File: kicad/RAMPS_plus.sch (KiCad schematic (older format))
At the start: 7 parts

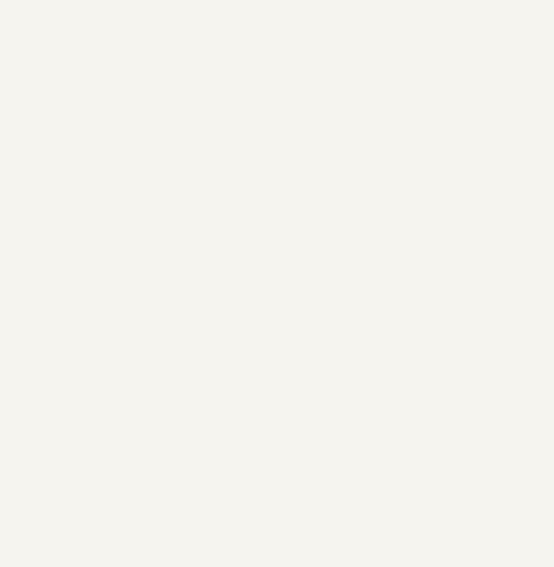
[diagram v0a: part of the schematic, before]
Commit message: Draw schematic
Added 40109 translators to drive MOSFET's.

References: #1 #5 #13 #9
Close #6
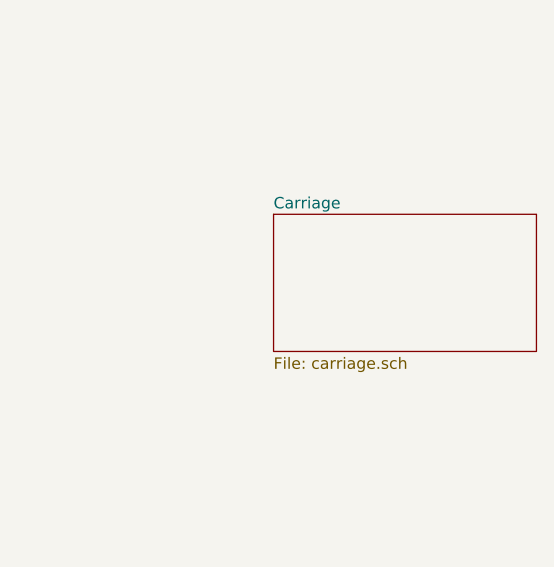
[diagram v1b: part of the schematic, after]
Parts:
- gave numbers to parts that had none: 7
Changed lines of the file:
@@
 EESchema Schematic File Version 2
 LIBS:CircuitHub
+LIBS:power
+LIBS:transistors
+LIBS:regul
+LIBS:device
 LIBS:RAMPS_plus-cache
 EELAYER 27 0
@@
 $Descr A4 11693 8268
 encoding utf-8
-Sheet 1 1
+Sheet 1 2
 Title "Ramps plus"
-Date "8 apr 2014"
+Date "15 apr 2014"
 Rev "1.0"
 Comp "peter@7408hacks.com"
@@
 $EndDescr
 $Comp
-L "1788-61300811121" P?
+L "1788-61300811121" P2
 U 1 1 53430C34
 P 2400 1600
-F 0 "P?" H 2400 1630 60  0000 L CNN
+F 0 "P2" H 2400 1630 60  0000 L CNN
 F 1 "\"1788-61300811121\"" H 2400 670 60  0000 L CNN
 F 2 "7408hacks/dibfv" H 2400 1900 60  0001 L CNN
@@
 $EndComp
 $Comp
-L "1788-61300811121" P?
+L "1788-61300811121" P3
 U 1 1 53430C53
 P 2400 2700
-F 0 "P?" H 2400 2730 60  0000 L CNN
+F 0 "P3" H 2400 2730 60  0000 L CNN
 F 1 "\"1788-61300811121\"" H 2400 1770 60  0000 L CNN
 F 2 "7408hacks/dibfv" H 2400 3000 60  0001 L CNN
@@
 $EndComp
 $Comp
-L "1788-61300811121" P?
+L "1788-61300811121" P4
 U 1 1 53430C72
 P 2400 3800
-F 0 "P?" H 2400 3830 60  0000 L CNN
+F 0 "P4" H 2400 3830 60  0000 L CNN
 F 1 "\"1788-61300811121\"" H 2400 2870 60  0000 L CNN
 F 2 "7408hacks/dibfv" H 2400 4100 60  0001 L CNN
@@
 $EndComp
 $Comp
-L "1788-61300811121" P?
+L "1788-61300811121" P6
 U 1 1 53430C91
 P 2700 2700
-F 0 "P?" H 2700 2730 60  0000 L CNN
+F 0 "P6" H 2700 2730 60  0000 L CNN
 F 1 "\"1788-61300811121\"" H 2700 1770 60  0000 L CNN
 F 2 "7408hacks/dibfv" H 2700 3000 60  0001 L CNN
@@
 $EndComp
 $Comp
-L "1788-61300811121" P?
+L "1788-61300811121" P7
 U 1 1 53430CB0
 P 2700 3800
-F 0 "P?" H 2700 3830 60  0000 L CNN
+F 0 "P7" H 2700 3830 60  0000 L CNN
 F 1 "\"1788-61300811121\"" H 2700 2870 60  0000 L CNN
 F 2 "7408hacks/dibfv" H 2700 4100 60  0001 L CNN
@@
 $EndComp
 $Comp
-L "1789-61301011121" P?
+L "1789-61301011121" P5
 U 1 1 53430CCF
 P 2700 1400
-F 0 "P?" H 2700 1430 60  0000 L CNN
+F 0 "P5" H 2700 1430 60  0000 L CNN
 F 1 "\"1789-61301011121\"" H 2700 270 60  0000 L CNN
 F 2 "7408hacks/dio2r" H 2700 1700 60  0001 L CNN
@@
 $EndComp
 $Comp
-L "1790-61303621121" P?
+L "1790-61303621121" P1
 U 1 1 534310C0
 P 2200 4900
-F 0 "P?" H 2200 4930 60  0000 L CNN
+F 0 "P1" H 2200 4930 60  0000 L CNN
 F 1 "\"1790-61303621121\"" H 2200 2970 60  0000 L CNN
 F 2 "7408hacks/dio2z" H 2200 5200 60  0001 L CNN
@@
 Wire Notes Line
 	3850 1050 1200 1050
+$Sheet
+S 5200 2000 1150 600
+U 534454B0
+F0 "Carriage" 50
+F1 "carriage.sch" 50
+$EndSheet
 $EndSCHEMATC

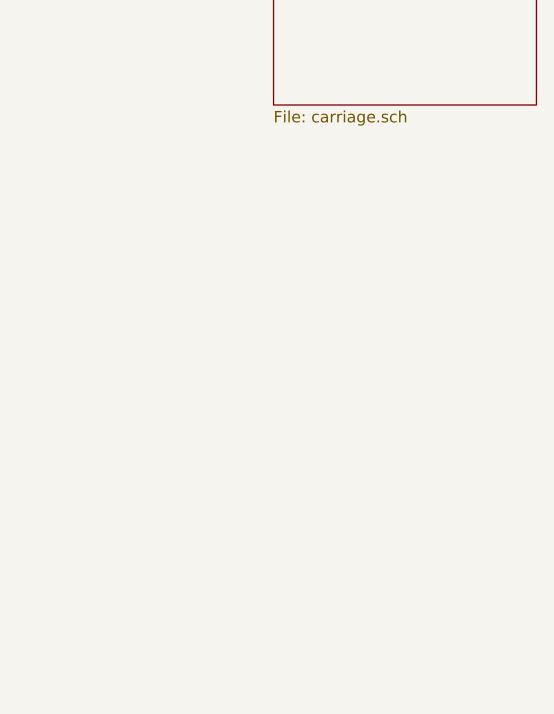
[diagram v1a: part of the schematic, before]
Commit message: Draw schematic
Added sheet for panel connector and sheet for Y axis circuits.
Added ULN2803

References: #1 #11 #7 #5
Close #13
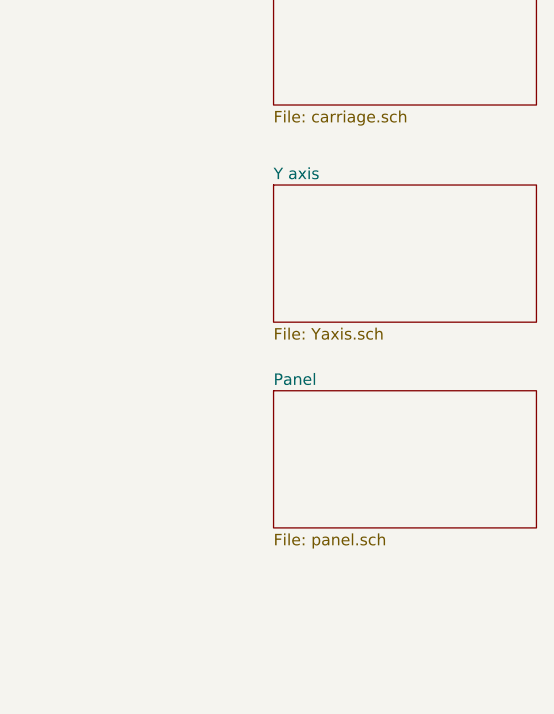
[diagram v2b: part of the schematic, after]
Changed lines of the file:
@@
 LIBS:CircuitHub
 LIBS:power
-LIBS:transistors
 LIBS:regul
 LIBS:device
+LIBS:opto
+LIBS:transistor
 LIBS:RAMPS_plus-cache
 EELAYER 27 0
@@
 $Descr A4 11693 8268
 encoding utf-8
-Sheet 1 2
+Sheet 1 4
 Title "Ramps plus"
-Date "15 apr 2014"
+Date "16 apr 2014"
 Rev "1.0"
 Comp "peter@7408hacks.com"
@@
 F1 "carriage.sch" 50
 $EndSheet
+$Sheet
+S 5200 2950 1150 600
+U 534EC4C7
+F0 "Y axis" 50
+F1 "Yaxis.sch" 50
+$EndSheet
+$Sheet
+S 5200 3850 1150 600
+U 534EE32B
+F0 "Panel" 50
+F1 "panel.sch" 50
+$EndSheet
 $EndSCHEMATC

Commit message: Draw schematic
Finished redrawing basic RAMPS schematic

References: #1 #4 #7 #15
Close #5 #17 #18
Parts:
- added C11, C12, C13: 100n/50V, 0603, symbol C
- added D5: N.C., 7408hacks/dibfu, symbol "1851-SS54"
- added D6, D7, D8, D9: \"1851-SS54\", 7408hacks/dibfu, symbol "1851-SS54"
- added F1, F2, F3, F4: FUSE, symbol FUSE
- added P18: CONN_6, symbol CONN_6
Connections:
- net labels added: +12V, Vbed, Vheat, Vmot
- wire segments 77 -> 117
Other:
- note added: "Littelfuse MINI Blade Fuse\nmodel 0297015 (15A)\n% of rating | opening time max\n135% | 600s\n200% | 5 s \n350% | 0.25 s \n600% | 0.1 s"

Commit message: Change components to my own
References: #1 #19
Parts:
- removed D5: N.C., 7408hacks/dibfu, symbol "1851-SS54"
- removed D6, D7, D8, D9: \"1851-SS54\", 7408hacks/dibfu, symbol "1851-SS54"
- removed F1, F2, F3, F4: FUSE, symbol FUSE
- removed P1: \"1790-61303621121\", 7408hacks/dio2z, symbol "1790-61303621121"
- removed P18: CONN_6, symbol CONN_6
- removed P2, P3, P4, P6, P7: \"1788-61300811121\", 7408hacks/dibfv, symbol "1788-61300811121"
- removed P5: \"1789-61301011121\", 7408hacks/dio2r, symbol "1789-61301011121"
- added CON1: CON10, symbol CON10
- added CON2, CON3, CON4, CON5, CON6: CON8, symbol CON8
- added CON7: CON18x2, symbol CON18x2
- added CON?: CON6, symbol CON6
- added D1, D2, D3, D4, D5: SS54, SMC, symbol SS54
- added F1, F2, F3, F4: MINI_Blade_Fuse_Holder, Littlefuse_01530008, symbol MINI_Blade_Fuse_Holder
- renumbered C11 to C1, C12 to C2, C13 to C3
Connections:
- wire segments 117 -> 130
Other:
- note added: "Littelfuse MINI Blade Fuse\nmodel 0297015 (15A)\n% of rating | opening time max\n135% | 600s\n200% | 5 s \n350% | 0.25 s \n600% | 0.1 s\nReverse protection diode should \nwithstand at least 50A for 0.3s."
- note removed: "Littelfuse MINI Blade Fuse\nmodel 0297015 (15A)\n% of rating | opening time max\n135% | 600s\n200% | 5 s \n350% | 0.25 s \n600% | 0.1 s"

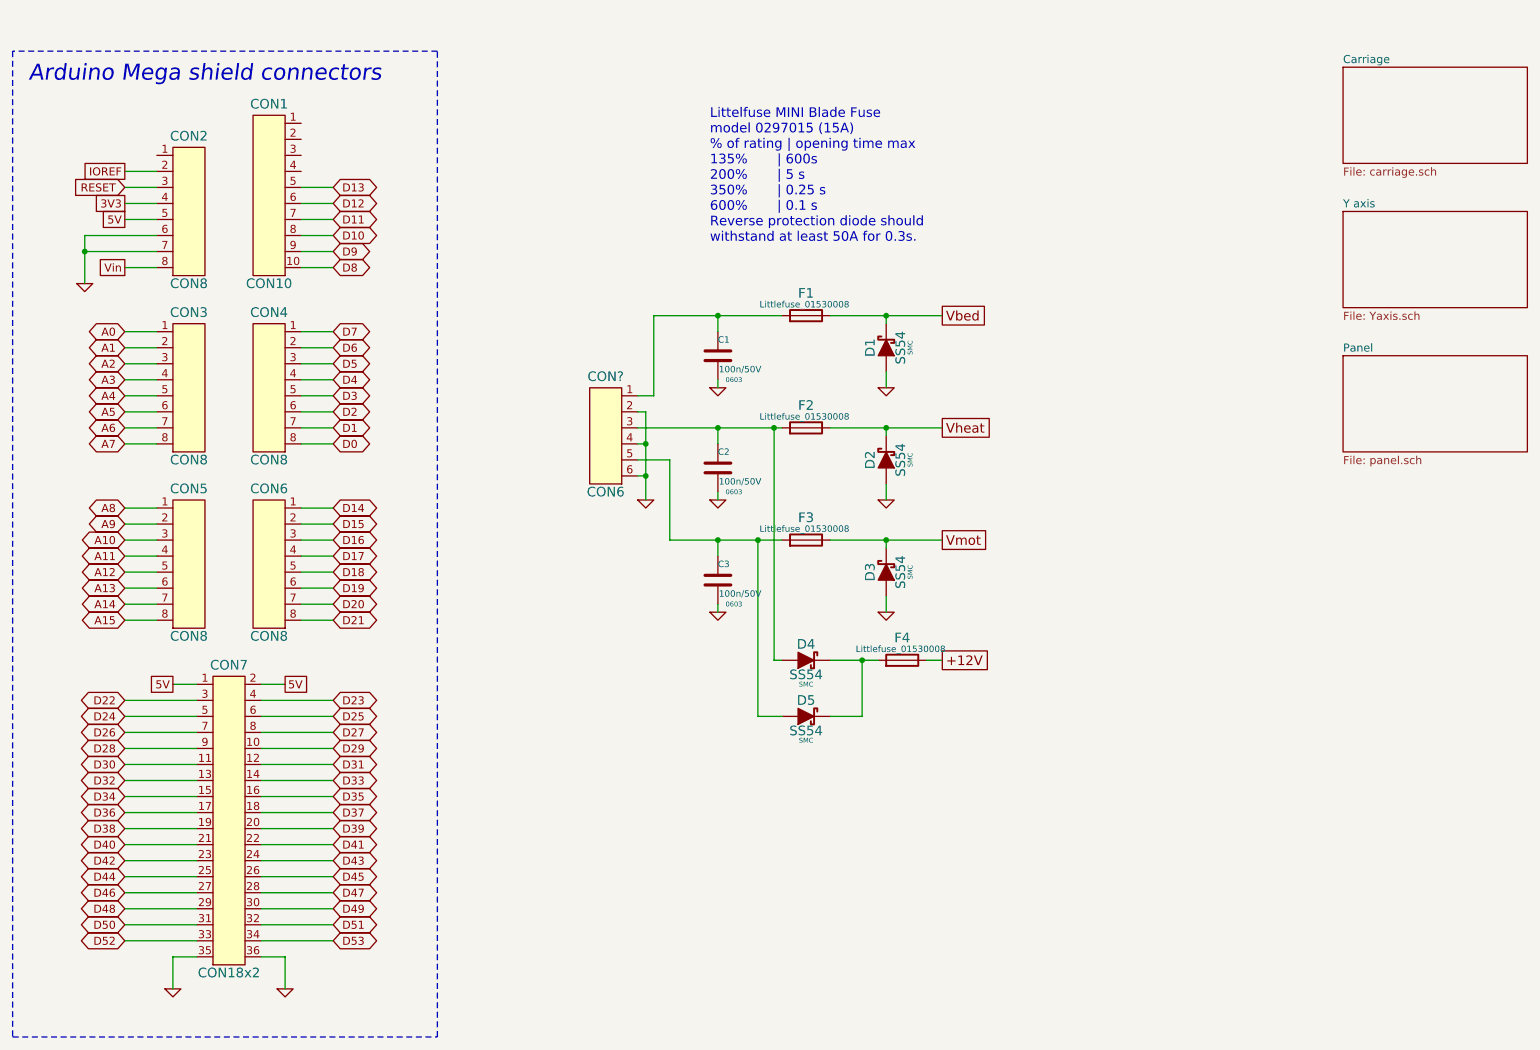
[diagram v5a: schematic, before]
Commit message: Add YZ connector. Add endstop filters.
Close #23
References: #3 #20
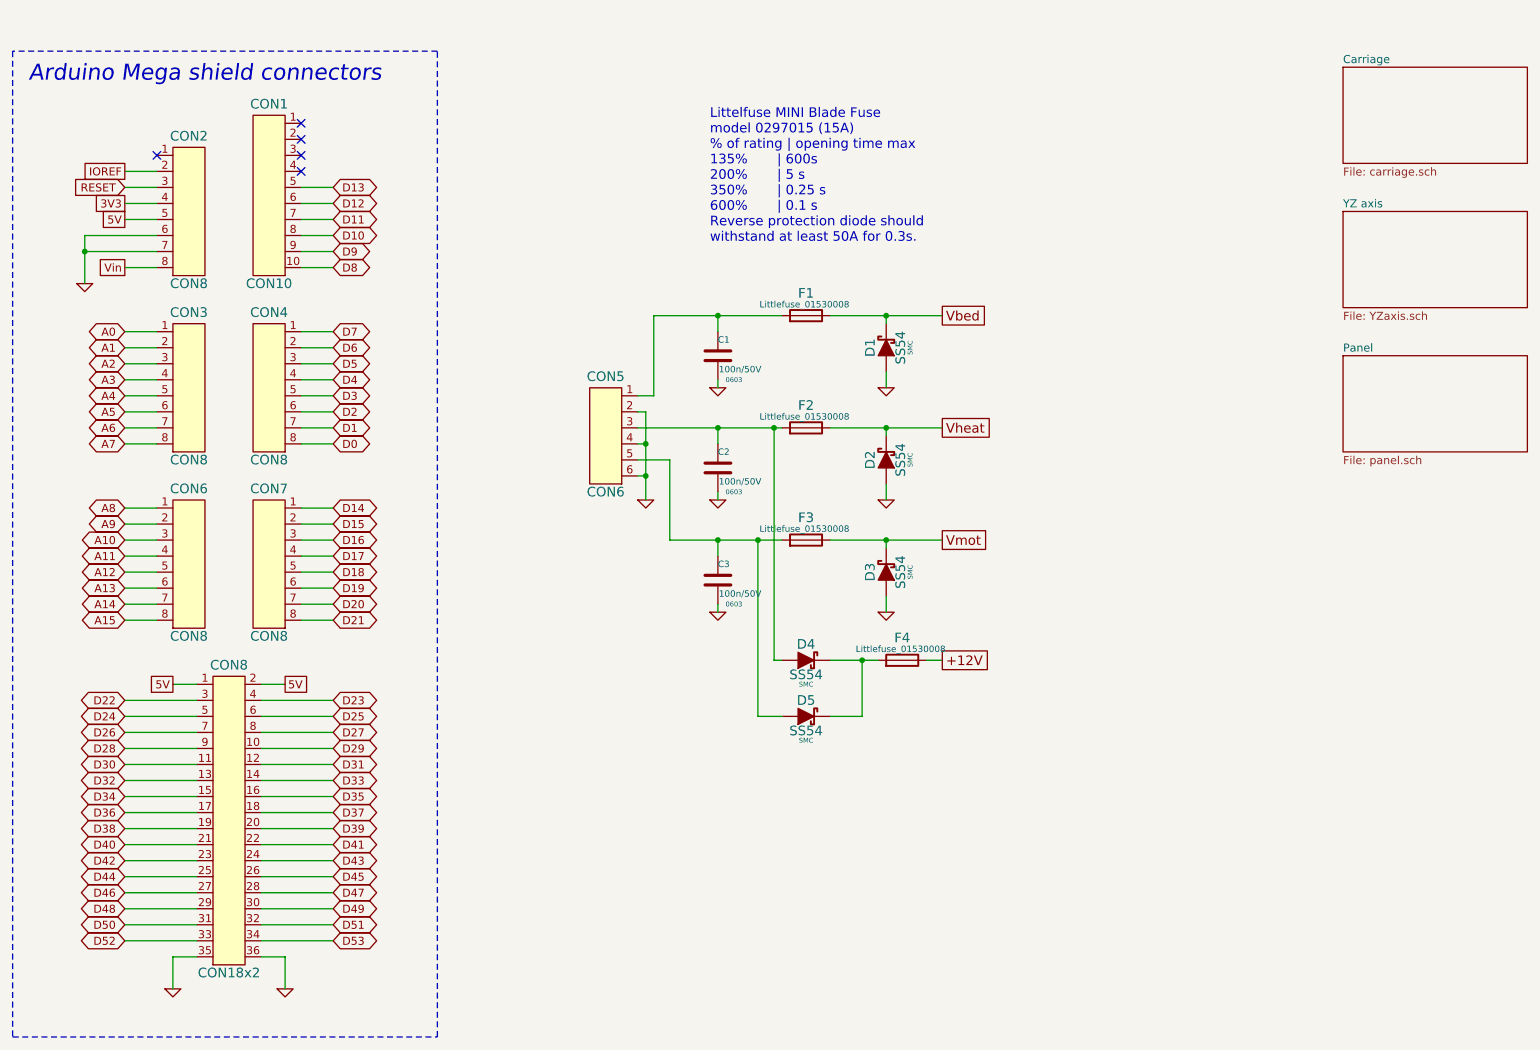
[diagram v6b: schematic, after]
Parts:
- gave numbers to parts that had none: 1
- renumbered CON5 to CON6, CON6 to CON7, CON7 to CON8
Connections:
- no-connect marks 0 -> 5
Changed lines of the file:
@@
 LIBS:pnSymbols
 LIBS:pnPins
+LIBS:pnModules
+LIBS:pnAnalogOther
+LIBS:pnLogic
 LIBS:RAMPS_plus-cache
 EELAYER 24 0
@@
 S 9500 2050 1150 600
 U 534EC4C7
-F0 "Y axis" 50
-F1 "Yaxis.sch" 50
+F0 "YZ axis" 50
+F1 "YZaxis.sch" 50
 $EndSheet
 $Sheet
@@
 $EndSheet
 $Comp
-L GND #PWR4
+L GND #PWR01
 U 1 1 536D3025
 P 5150 3850
-F 0 "#PWR4" H 5150 3850 30  0001 C CNN
+F 0 "#PWR01" H 5150 3850 30  0001 C CNN
 F 1 "GND" H 5150 3780 30  0001 C CNN
 F 2 "" H 5150 3850 60  0000 C CNN
@@
 Littelfuse MINI Blade Fuse\nmodel 0297015 (15A)\n% of rating | opening time max\n135%       | 600s\n200%       | 5 s \n350%       | 0.25 s \n600%       | 0.1 s\nReverse protection diode should \nwithstand at least 50A for 0.3s.
 $Comp
-L GND #PWR6
+L GND #PWR02
 U 1 1 536D3E3D
 P 6650 3850
-F 0 "#PWR6" H 6650 3850 30  0001 C CNN
+F 0 "#PWR02" H 6650 3850 30  0001 C CNN
 F 1 "GND" H 6650 3780 30  0001 C CNN
 F 2 "" H 6650 3850 60  0000 C CNN
@@
 $EndComp
 $Comp
-L GND #PWR3
+L GND #PWR03
 U 1 1 536D3E48
 P 6650 3150
-F 0 "#PWR3" H 6650 3150 30  0001 C CNN
+F 0 "#PWR03" H 6650 3150 30  0001 C CNN
 F 1 "GND" H 6650 3080 30  0001 C CNN
 F 2 "" H 6650 3150 60  0000 C CNN
@@
 $EndComp
 $Comp
-L GND #PWR8
+L GND #PWR04
 U 1 1 536D3E53
 P 6650 4550
-F 0 "#PWR8" H 6650 4550 30  0001 C CNN
+F 0 "#PWR04" H 6650 4550 30  0001 C CNN
 F 1 "GND" H 6650 4480 30  0001 C CNN
 F 2 "" H 6650 4550 60  0000 C CNN
@@
 $EndComp
 $Comp
-L GND #PWR2
+L GND #PWR05
 U 1 1 536D4137
 P 5600 3150
-F 0 "#PWR2" H 5600 3150 30  0001 C CNN
+F 0 "#PWR05" H 5600 3150 30  0001 C CNN
 F 1 "GND" H 5600 3080 30  0001 C CNN
 F 2 "" H 5600 3150 60  0000 C CNN
@@
 $EndComp
 $Comp
-L GND #PWR5
+L GND #PWR06
 U 1 1 536D4142
 P 5600 3850
-F 0 "#PWR5" H 5600 3850 30  0001 C CNN
+F 0 "#PWR06" H 5600 3850 30  0001 C CNN
 F 1 "GND" H 5600 3780 30  0001 C CNN
 F 2 "" H 5600 3850 60  0000 C CNN
@@
 $EndComp
 $Comp
-L GND #PWR7
+L GND #PWR07
 U 1 1 536D414D
 P 5600 4550
-F 0 "#PWR7" H 5600 4550 30  0001 C CNN
+F 0 "#PWR07" H 5600 4550 30  0001 C CNN
 F 1 "GND" H 5600 4480 30  0001 C CNN
 F 2 "" H 5600 4550 60  0000 C CNN
@@
 	5100 3300 5150 3300
 Wire Wire Line
-	5150 3300 5150 3500
-Wire Wire Line
-	5150 3500 5150 3700
-Wire Wire Line
-	5150 3700 5150 3850
+	5150 3300 5150 3850
 Wire Wire Line
 	5100 3500 5150 3500
 Connection ~ 5150 3500
 Wire Wire Line
-	5100 3400 5600 3400
-Wire Wire Line
-	5600 3400 5950 3400
-Wire Wire Line
-	5950 3400 6000 3400
+	5100 3400 6000 3400
 Wire Wire Line
 	5200 3200 5100 3200
@@
 	5300 3600 5300 4100
 Wire Wire Line
-	5300 4100 5600 4100
-Wire Wire Line
-	5600 4100 5850 4100
-Wire Wire Line
-	5850 4100 6000 4100
-Wire Wire Line
-	5200 2700 5600 2700
-Wire Wire Line
-	5600 2700 6000 2700
-Wire Wire Line
-	6300 3400 6650 3400
-Wire Wire Line
-	6650 3400 7000 3400
+	5300 4100 6000 4100
+Wire Wire Line
+	5200 2700 6000 2700
+Wire Wire Line
+	6300 3400 7000 3400
 Wire Wire Line
 	6650 3400 6650 3450
 Wire Wire Line
-	6300 2700 6650 2700
-Wire Wire Line
-	6650 2700 7000 2700
+	6300 2700 7000 2700
 Wire Wire Line
 	6650 2700 6650 2750
 Wire Wire Line
-	6300 4100 6650 4100
-Wire Wire Line
-	6650 4100 7000 4100
+	6300 4100 7000 4100
 Wire Wire Line
 	6650 4100 6650 4150
@@
 	5850 5200 6000 5200
 Wire Wire Line
-	6300 4850 6500 4850
-Wire Wire Line
-	6500 4850 6600 4850
+	6300 4850 6600 4850
 Wire Wire Line
 	6300 5200 6500 5200
@@
 $EndComp
 $Comp
-L CON8 CON5
+L CON8 CON6
 U 1 1 536FA49C
 P 2300 4250
-F 0 "CON5" H 2300 4720 60  0000 C CNN
+F 0 "CON6" H 2300 4720 60  0000 C CNN
 F 1 "CON8" H 2300 3800 60  0000 C CNN
 F 2 "" H 2300 4250 40  0000 C CNN
@@
 $EndComp
 $Comp
-L CON8 CON6
+L CON8 CON7
 U 1 1 536FA4A7
 P 2800 4250
-F 0 "CON6" H 2800 4720 60  0000 C CNN
+F 0 "CON7" H 2800 4720 60  0000 C CNN
 F 1 "CON8" H 2800 3800 60  0000 C CNN
 F 2 "" H 2800 4250 40  0000 C CNN
@@
 $EndComp
 $Comp
-L CON18x2 CON7
+L CON18x2 CON8
 U 1 1 536FA4DD
 P 2550 5850
-F 0 "CON7" H 2550 6820 60  0000 C CNN
+F 0 "CON8" H 2550 6820 60  0000 C CNN
 F 1 "CON18x2" H 2550 4900 60  0000 C CNN
 F 2 "" H 2550 5850 40  0000 C CNN
@@
 $EndComp
 $Comp
-L GND #PWR1
+L GND #PWR08
 U 1 1 536FA4F6
 P 1650 2500
-F 0 "#PWR1" H 1650 2500 30  0001 C CNN
+F 0 "#PWR08" H 1650 2500 30  0001 C CNN
 F 1 "GND" H 1650 2430 30  0001 C CNN
 F 2 "" H 1650 2500 60  0000 C CNN
@@
 $EndComp
 Wire Wire Line
-	1650 2200 1650 2300
-Wire Wire Line
-	1650 2300 1650 2500
+	1650 2200 1650 2500
 Connection ~ 1650 2300
 Wire Wire Line
@@
 	2200 6700 2350 6700
 $Comp
-L GND #PWR10
+L GND #PWR09
 U 1 1 536FA739
 P 2900 6900
-F 0 "#PWR10" H 2900 6900 30  0001 C CNN
+F 0 "#PWR09" H 2900 6900 30  0001 C CNN
 F 1 "GND" H 2900 6830 30  0001 C CNN
 F 2 "" H 2900 6900 60  0000 C CNN
@@
 	2350 5000 2200 5000
 $Comp
-L GND #PWR9
+L GND #PWR010
 U 1 1 536FA866
 P 2200 6900
-F 0 "#PWR9" H 2200 6900 30  0001 C CNN
+F 0 "#PWR010" H 2200 6900 30  0001 C CNN
 F 1 "GND" H 2200 6830 30  0001 C CNN
 F 2 "" H 2200 6900 60  0000 C CNN
@@
 	2900 6700 2900 6900
 $Comp
-L CON6 CON?
+L CON6 CON5
 U 1 1 536FABD7
 P 4900 3450
-F 0 "CON?" H 4900 3820 60  0000 C CNN
+F 0 "CON5" H 4900 3820 60  0000 C CNN
 F 1 "CON6" H 4900 3100 60  0000 C CNN
 F 2 "" H 4900 3450 40  0000 C CNN
@@
 	-1   0    0    -1
 $EndComp
+NoConn ~ 2100 1700
+NoConn ~ 3000 1500
+NoConn ~ 3000 1600
+NoConn ~ 3000 1700
+NoConn ~ 3000 1800
 $EndSCHEMATC
